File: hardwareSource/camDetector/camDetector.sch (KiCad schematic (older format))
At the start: 12 parts, among them J3 USB_B_Micro

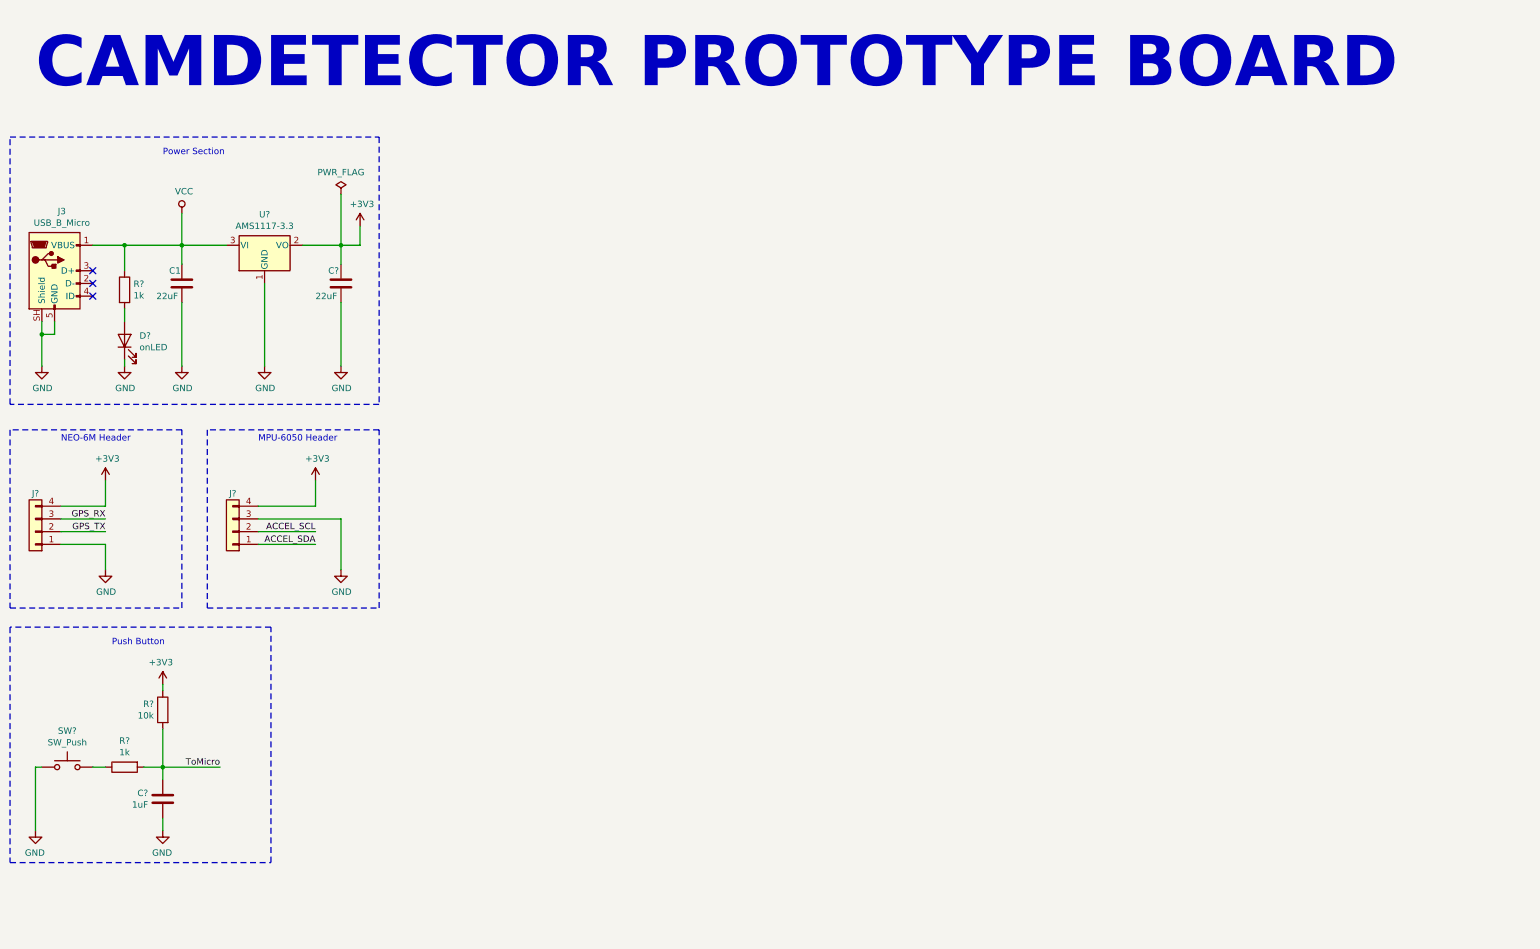
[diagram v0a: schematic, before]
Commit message: added esp32 header
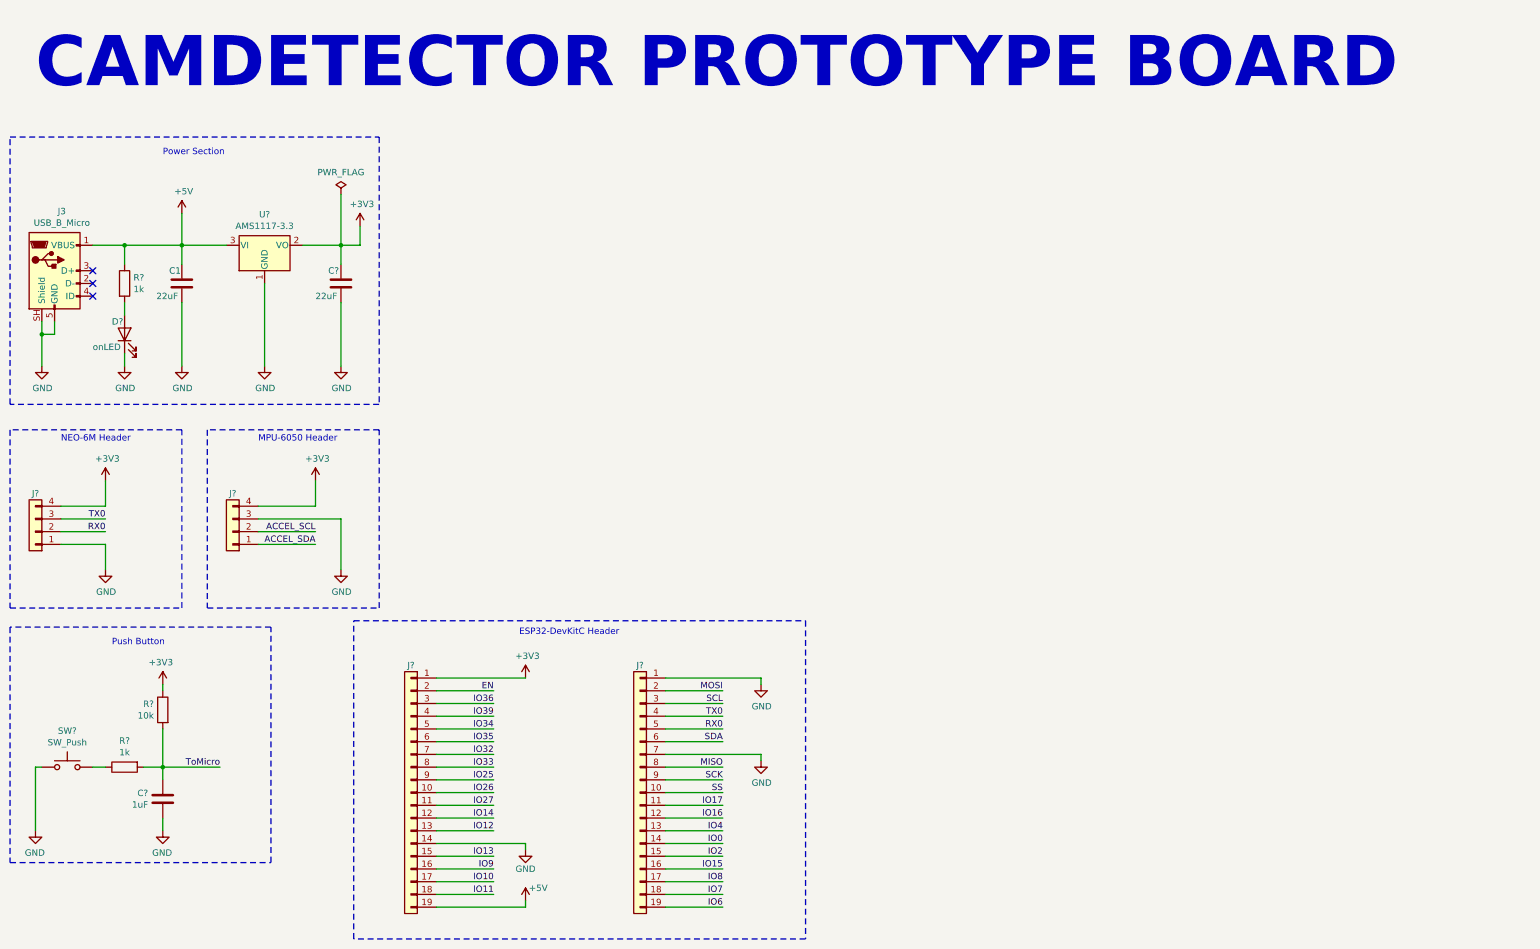
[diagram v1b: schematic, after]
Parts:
- added J? (x2): Conn_01x19, symbol Connector_Generic:Conn_01x19
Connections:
- net +3V3: now also J?.1 (Pin_1)
- net GND: now also J?.1 (Pin_1), J?.14 (Pin_14), J?.7 (Pin_7)
- net GPS_RX renamed TX0
- net TX0: now also J?.4 (Pin_4)
- net GPS_TX renamed RX0
- net RX0: now also J?.5 (Pin_5)
- net VCC renamed +5V
- net +5V: now also J?.19 (Pin_19)
- new net EN: J?.2 (Pin_2)
- new net IO0: J?.14 (Pin_14)
- new net IO10: J?.17 (Pin_17)
- new net IO11: J?.18 (Pin_18)
- new net IO12: J?.13 (Pin_13)
- new net IO13: J?.15 (Pin_15)
- new net IO14: J?.12 (Pin_12)
- new net IO15: J?.16 (Pin_16)
- new net IO16: J?.12 (Pin_12)
- new net IO17: J?.11 (Pin_11)
- new net IO2: J?.15 (Pin_15)
- new net IO25: J?.9 (Pin_9)
- new net IO26: J?.10 (Pin_10)
- new net IO27: J?.11 (Pin_11)
- new net IO32: J?.7 (Pin_7)
- new net IO33: J?.8 (Pin_8)
- new net IO34: J?.5 (Pin_5)
- new net IO35: J?.6 (Pin_6)
- new net IO36: J?.3 (Pin_3)
- new net IO39: J?.4 (Pin_4)
- new net IO4: J?.13 (Pin_13)
- new net IO6: J?.19 (Pin_19)
- new net IO7: J?.18 (Pin_18)
- new net IO8: J?.17 (Pin_17)
- new net IO9: J?.16 (Pin_16)
- new net MISO: J?.8 (Pin_8)
- new net MOSI: J?.2 (Pin_2)
- new net SCK: J?.9 (Pin_9)
- new net SCL: J?.3 (Pin_3)
- new net SDA: J?.6 (Pin_6)
- new net SS: J?.10 (Pin_10)
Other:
- note added: "ESP32-DevKitC Header\n\n"
- moved on the sheet: D?, R?
